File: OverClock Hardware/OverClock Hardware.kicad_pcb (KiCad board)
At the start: 4 copper layers, 100 x 100 mm, 126 parts, among them J1 USB_C_Plug, J2 JTAG_HDR, J3 Conn_01x03_Female, SW1 Switch_Momentary, SW2 Switch_Momentary, SW3 Switch_Momentary, SW4 Switch_Momentary, U1 TLV62569, U2 AP7365, U3 10M02SCE144

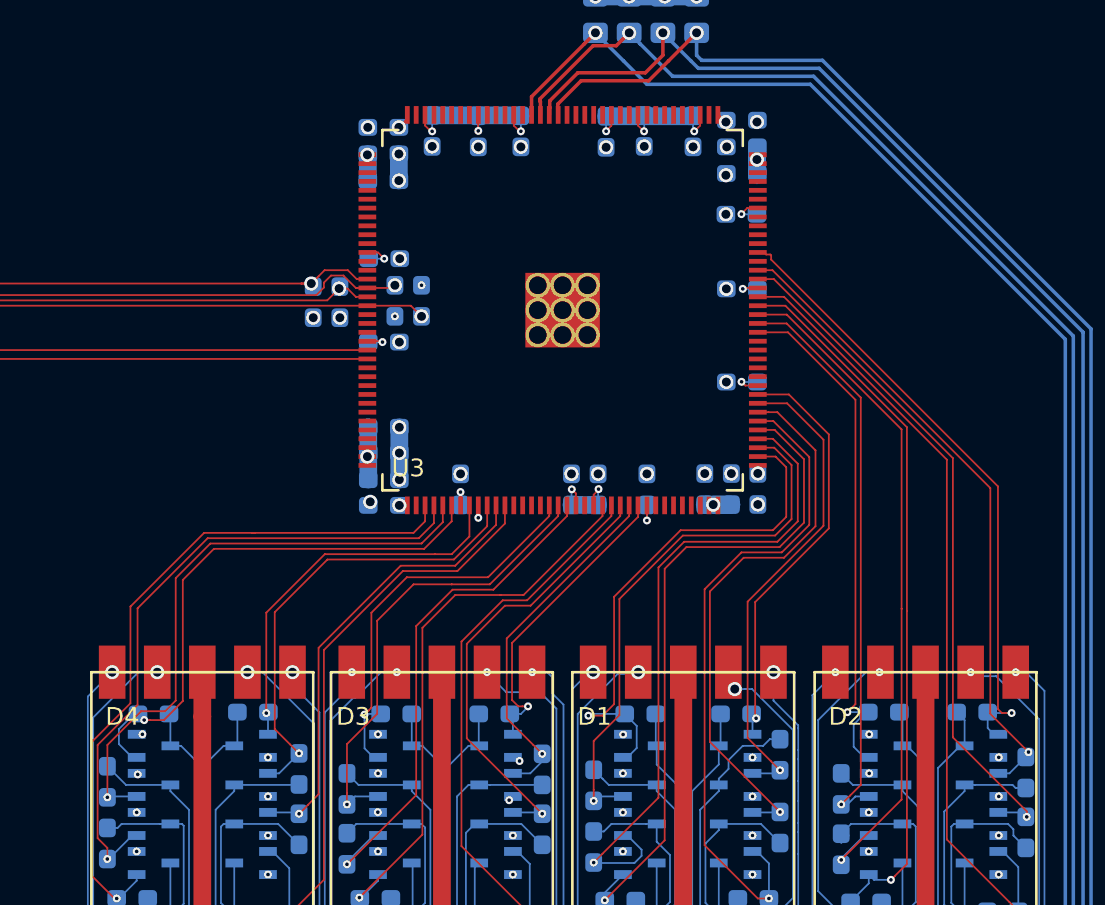
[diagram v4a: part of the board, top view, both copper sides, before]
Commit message: Cleaned up board to remove DRC Errors
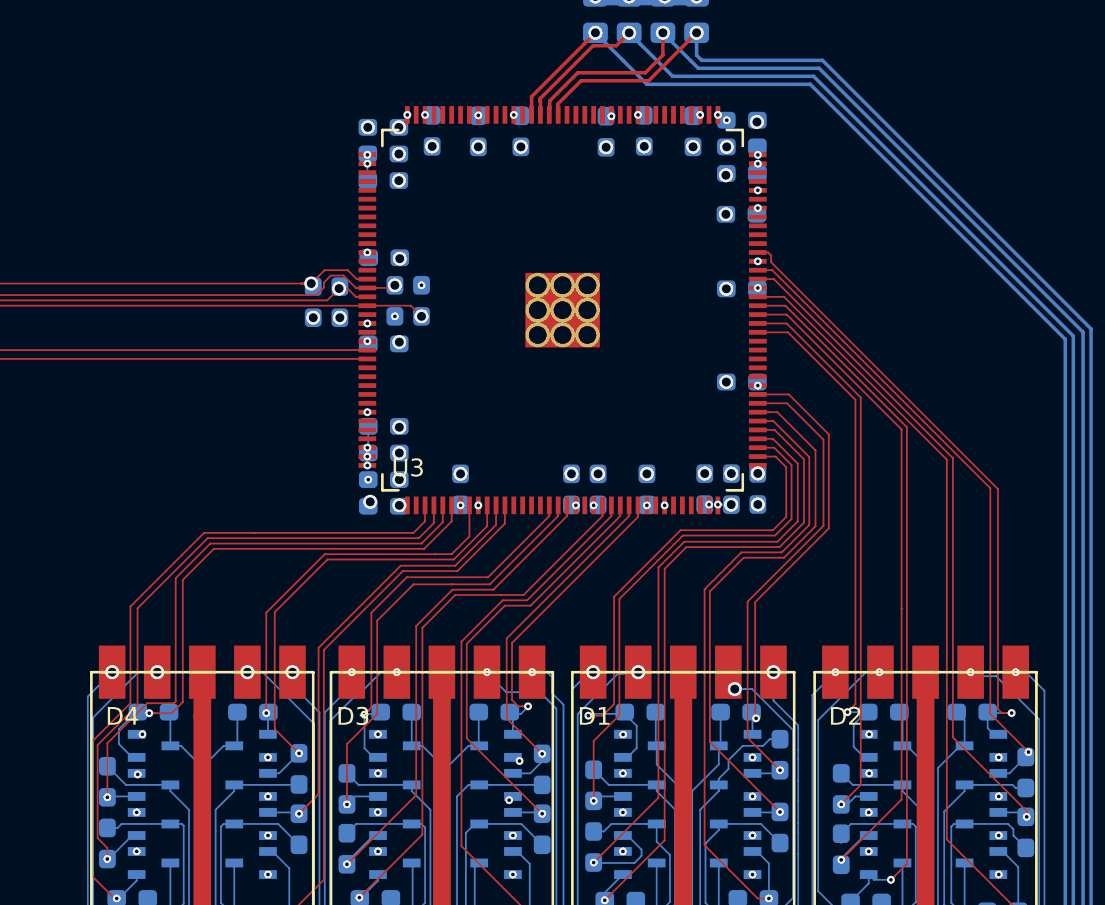
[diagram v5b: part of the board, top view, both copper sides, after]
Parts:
- moved R14 0.10 mm to (59.8, 42.6)
- moved R15 0.10 mm to (54.4, 42.6)
- moved R30 0.10 mm to (46.1, 42.6)
- moved R31 0.10 mm to (40.6, 42.6)
- moved R39 0.10 mm to (26.9, 42.6)
- moved C9 0.10 mm to (39.9, 21.9)
- moved C10 0.05 mm to (39.9, 26.6)
- moved C13 0.05 mm to (39.9, 31.1)
- moved C8 0.05 mm to (40.0, 17.1)
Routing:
- net +3V: track 60.1 -> 16.5 mm, vias 43 -> 52
- net GND: track 38.5 -> 33.4 mm, vias 98 -> 103
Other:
- net class Default: clearance 0.2 -> 0.1
- net class Power removed
- rule trace_clearance: 0.2 -> 0.1
- rule via_min_size: 0.2 -> 0.45
